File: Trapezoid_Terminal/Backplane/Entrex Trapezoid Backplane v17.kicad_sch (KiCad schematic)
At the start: 18 parts, among them J10 Conn_02x22_Odd_Even, J11 Floppy I/O, J12 Conn_02x15_Odd_Even, J13 Conn_02x15_Odd_Even, J14 Conn_02x15_Odd_Even, J15 Card Edge Connector, J16 Conn_02x50_Odd_Even, J17 trapezoid, J18 Card Edge Connector, J19 trapezoid, J20 trapezoid, J21 Conn_01x07_Pin, J22 Conn_02x12_Odd_Even, J24 Conn_01x08_Pin, J25 Mystery, J9 Conn_02x22_Odd_Even

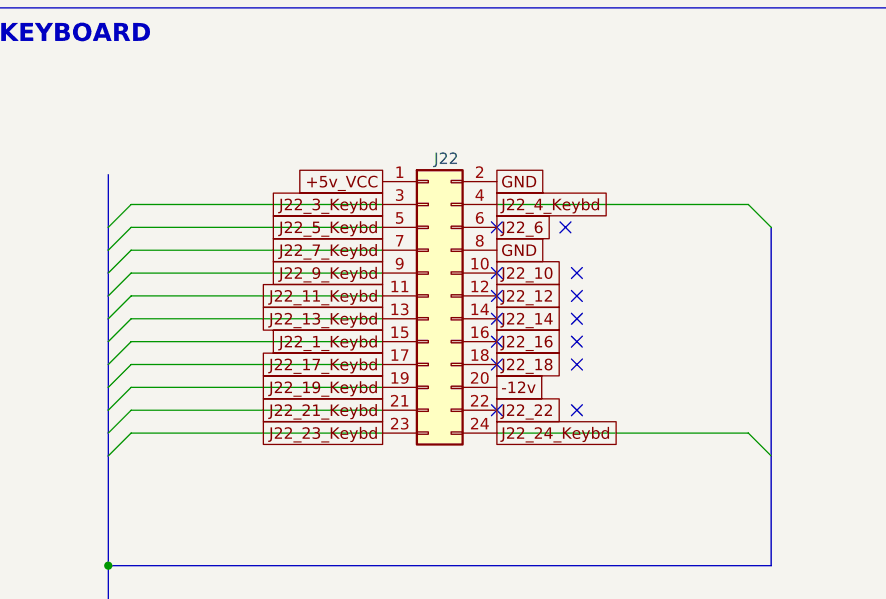
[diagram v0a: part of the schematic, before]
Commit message: Add Keyboard Plug Mapping
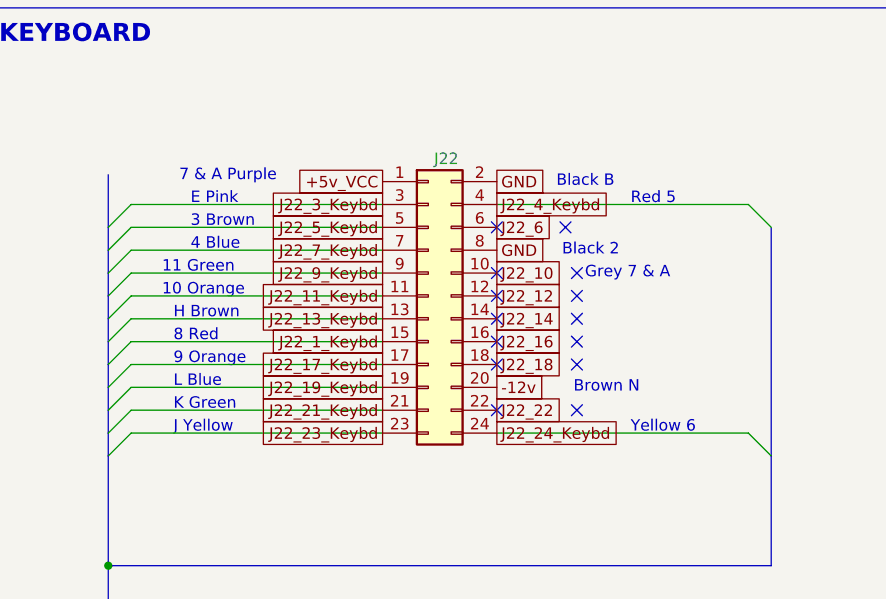
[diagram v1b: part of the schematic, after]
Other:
- note added: "10 Orange"
- note added: "11 Green"
- note added: "3 Brown"
- note added: "4 Blue"
- note added: "7 & A Purple"
- note added: "8 Red"
- note added: "9 Orange"
- note added: "Black 2"
- note added: "Black B"
- note added: "Brown N"
- note added: "E Pink"
- note added: "Grey 7 & A"
- note added: "H Brown"
- note added: "J Yellow"
- note added: "K Green"
- note added: "L Blue"
- note added: "Red 5"
- note added: "Yellow 6"
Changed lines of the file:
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@@
     (effects (font (size 2 2) bold) (justify left top))
+  )
+  (text "Black 2" (at 951.23 148.59 0)
+    (effects (font (size 1.27 1.27) (color 0 0 0 1)) (justify left bottom))
   )
   (text "*" (at 331.597 77.724 0)
@@
   (text "RAM Bus" (at 615.188 277.622 0)
     (effects (font (size 2 2) (thickness 0.4) bold) (justify left bottom))
+  )
+  (text "7 & A Purple" (at 908.685 140.335 0)
+    (effects (font (size 1.27 1.27) (color 128 0 128 1)) (justify left bottom))
   )
   (text "To Interface\nBoard Only" (at 597.408 106.807 0)
@@
     (effects (font (size 1.27 1.27) (color 255 30 30 1)) (justify left bottom))
   )
+  (text "Yellow 6" (at 958.85 168.275 0)
+    (effects (font (size 1.27 1.27) (color 255 255 0 1)) (justify left bottom))
+  )
+  (text "Brown N" (at 952.5 163.83 0)
+    (effects (font (size 1.27 1.27) (color 150 75 0 1)) (justify left bottom))
+  )
   (text "*" (at 449.199 211.328 0)
     (effects (font (size 3 3) (thickness 1) bold (color 0 0 0 1)) (justify right bottom))
+  )
+  (text "K Green\n" (at 908.05 165.735 0)
+    (effects (font (size 1.27 1.27) (color 0 100 0 1)) (justify left bottom))
   )
   (text "to J25_17" (at 666.115 202.692 0)
@@
     (effects (font (size 3 3) (thickness 1) bold (color 255 38 190 1)) (justify right bottom))
   )
+  (text "9 Orange" (at 908.05 160.655 0)
+    (effects (font (size 1.27 1.27) (color 255 165 0 1)) (justify left bottom))
+  )
+  (text "H Brown" (at 908.05 155.575 0)
+    (effects (font (size 1.27 1.27) (color 150 75 0 1)) (justify left bottom))
+  )
+  (text "Red 5" (at 958.85 142.875 0)
+    (effects (font (size 1.27 1.27) (color 255 0 0 1)) (justify left bottom))
+  )
   (text "*" (at 483.743 211.328 0)
     (effects (font (size 3 3) (thickness 1) bold (color 255 165 0 1)) (justify right bottom))
+  )
+  (text "L Blue" (at 908.05 163.195 0)
+    (effects (font (size 1.27 1.27) (color 0 0 255 1)) (justify left bottom))
+  )
+  (text "Grey 7 & A" (at 953.77 151.13 0)
+    (effects (font (size 1.27 1.27) (color 128 128 128 1)) (justify left bottom))
   )
   (text "*" (at 790.067 207.264 0)
@@
   (text "*" (at 451.739 211.328 0)
     (effects (font (size 3 3) (thickness 1) bold (color 255 38 190 1)) (justify right bottom))
+  )
+  (text "E Pink\n" (at 909.955 142.875 0)
+    (effects (font (size 1.27 1.27) (color 255 192 203 1)) (justify left bottom))
   )
   (text "to J25\n" (at 630.301 320.548 0)
@@
   (text "*" (at 787.527 207.264 0)
     (effects (font (size 3 3) (thickness 1) bold (color 255 38 190 1)) (justify right bottom))
+  )
+  (text "3 Brown" (at 909.955 145.415 0)
+    (effects (font (size 1.27 1.27) (color 150 75 0 1)) (justify left bottom))
+  )
+  (text "4 Blue" (at 909.955 147.955 0)
+    (effects (font (size 1.27 1.27) (color 0 0 255 1)) (justify left bottom))
   )
   (text "B\nC\nF\nA\nP\nJ\nH\nR\nD\nN\n" (at 151.13 139.446 0)
@@
     (effects (font (size 3 3) (thickness 1) bold (color 18 244 255 1)) (justify right bottom))
   )
+  (text "J Yellow" (at 908.05 168.275 0)
+    (effects (font (size 1.27 1.27) (color 255 255 0 1)) (justify left bottom))
+  )
+  (text "11 Green\n" (at 906.78 150.495 0)
+    (effects (font (size 1.27 1.27) (color 0 100 0 1)) (justify left bottom))
+  )
   (text "to J25\n" (at 630.301 302.768 0)
     (effects (font (size 1.27 1.27)) (justify left bottom))
@@
     (effects (font (size 1.27 1.27)) (justify left bottom))
   )
+  (text "Black B" (at 950.595 140.97 0)
+    (effects (font (size 1.27 1.27) (color 0 0 0 1)) (justify left bottom))
+  )
+  (text "10 Orange" (at 906.78 153.035 0)
+    (effects (font (size 1.27 1.27) (color 255 165 0 1)) (justify left bottom))
+  )
   (text "*" (at 331.597 53.594 0)
     (effects (font (size 3 3) (thickness 1) bold (color 5 102 8 1)) (justify right bottom))
@@
     (effects (font (size 1.27 1.27)) (justify left bottom))
   )
+  (text "8 Red" (at 908.05 158.115 0)
+    (effects (font (size 1.27 1.27) (color 255 0 0 1)) (justify left bottom))
+  )
   (label "J10_16_Prntr" (at 502.793 140.97 0) (fields_autoplaced)
